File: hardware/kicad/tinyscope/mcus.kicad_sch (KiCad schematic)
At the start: 22 parts, among them SW1 SW_SPST, U10 STM32H753VITx, X1 25MHz

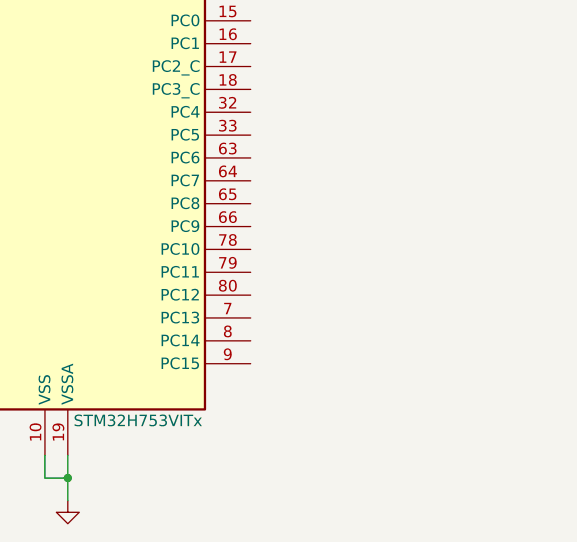
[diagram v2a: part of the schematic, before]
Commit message: feat: hardware: Add tinyscope kicad project. Adds LSE XTAL. Missing capacitor values
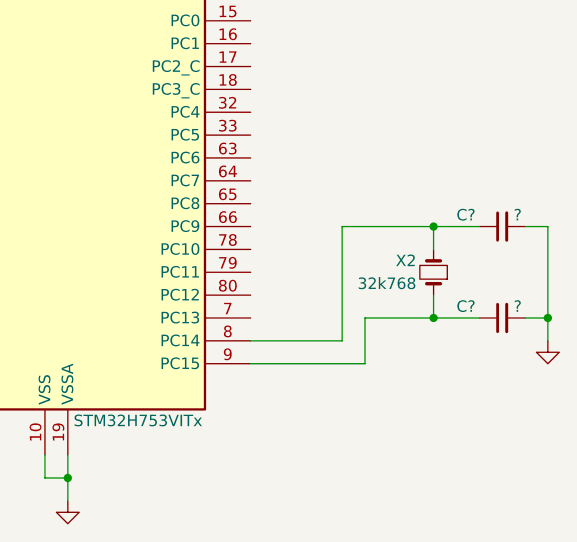
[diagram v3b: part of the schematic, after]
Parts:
- added C? (x2): ?, symbol Device:C_Small
- added X2: 32k768, symbol Device:Crystal_Small
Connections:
- net GND: now also C?.2, C?.2
- net at U10.8 (PC14): now also C?.1, X2.2
- net at U10.9 (PC15): now also C?.1, X2.1
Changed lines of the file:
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@@
   (junction (at 83.82 60.96) (diameter 0) (color 0 0 0 0)
   )
+  (junction (at 175.26 160.02) (diameter 0) (color 0 0 0 0)
+  )
   (junction (at 50.8 33.02) (diameter 0) (color 0 0 0 0)
   )
@@
   (junction (at 71.12 33.02) (diameter 0) (color 0 0 0 0)
   )
+  (junction (at 187.96 160.02) (diameter 0) (color 0 0 0 0)
+  )
   (junction (at 40.64 22.86) (diameter 0) (color 0 0 0 0)
   )
@@
   (junction (at 60.96 22.86) (diameter 0) (color 0 0 0 0)
   )
+  (junction (at 175.26 149.86) (diameter 0) (color 0 0 0 0)
+  )
   (junction (at 157.48 22.86) (diameter 0) (color 0 0 0 0)
   )
@@
     (stroke (width 0) (type default))
   )
+  (wire (pts (xy 175.26 149.86) (xy 180.34 149.86))
+    (stroke (width 0) (type default))
+  )
   (wire (pts (xy 40.64 33.02) (xy 30.48 33.02))
     (stroke (width 0) (type default))
   )
+  (wire (pts (xy 185.42 149.86) (xy 187.96 149.86))
+    (stroke (width 0) (type default))
+  )
   (wire (pts (xy 55.88 58.42) (xy 55.88 60.96))
     (stroke (width 0) (type default))
@@
     (stroke (width 0) (type default))
   )
+  (wire (pts (xy 187.96 149.86) (xy 187.96 160.02))
+    (stroke (width 0) (type default))
+  )
   (wire (pts (xy 30.48 40.64) (xy 30.48 45.72))
     (stroke (width 0) (type default))
@@
     (stroke (width 0) (type default))
   )
+  (wire (pts (xy 175.26 160.02) (xy 180.34 160.02))
+    (stroke (width 0) (type default))
+  )
   (wire (pts (xy 134.62 175.26) (xy 134.62 177.8))
     (stroke (width 0) (type default))
@@
     (stroke (width 0) (type default))
   )
+  (wire (pts (xy 187.96 160.02) (xy 187.96 162.56))
+    (stroke (width 0) (type default))
+  )
+  (wire (pts (xy 175.26 149.86) (xy 175.26 152.4))
+    (stroke (width 0) (type default))
+  )
   (wire (pts (xy 157.48 33.02) (xy 167.64 33.02))
     (stroke (width 0) (type default))
   )
+  (wire (pts (xy 175.26 157.48) (xy 175.26 160.02))
+    (stroke (width 0) (type default))
+  )
+  (wire (pts (xy 154.94 162.56) (xy 165.1 162.56))
+    (stroke (width 0) (type default))
+  )
   (wire (pts (xy 50.8 22.86) (xy 50.8 25.4))
     (stroke (width 0) (type default))
@@
     (stroke (width 0) (type default))
   )
+  (wire (pts (xy 165.1 149.86) (xy 165.1 162.56))
+    (stroke (width 0) (type default))
+  )
   (wire (pts (xy 96.52 162.56) (xy 96.52 165.1))
     (stroke (width 0) (type default))
@@
     (stroke (width 0) (type default))
   )
+  (wire (pts (xy 175.26 160.02) (xy 167.64 160.02))
+    (stroke (width 0) (type default))
+  )
   (wire (pts (xy 99.06 30.48) (xy 109.22 30.48))
     (stroke (width 0) (type default))
@@
     (stroke (width 0) (type default))
   )
+  (wire (pts (xy 167.64 160.02) (xy 167.64 165.1))
+    (stroke (width 0) (type default))
+  )
   (wire (pts (xy 93.98 53.34) (xy 96.52 53.34))
     (stroke (width 0) (type default))
@@
     (stroke (width 0) (type default))
   )
+  (wire (pts (xy 175.26 149.86) (xy 165.1 149.86))
+    (stroke (width 0) (type default))
+  )
   (wire (pts (xy 106.68 160.02) (xy 106.68 162.56))
     (stroke (width 0) (type default))
@@
     (stroke (width 0) (type default))
   )
+  (wire (pts (xy 185.42 160.02) (xy 187.96 160.02))
+    (stroke (width 0) (type default))
+  )
   (wire (pts (xy 66.04 58.42) (xy 66.04 60.96))
     (stroke (width 0) (type default))
@@
   )
   (wire (pts (xy 71.12 33.02) (xy 71.12 30.48))
+    (stroke (width 0) (type default))
+  )
+  (wire (pts (xy 167.64 165.1) (xy 154.94 165.1))
     (stroke (width 0) (type default))
   )
@@
     )
   )
+  (symbol (lib_id "Device:Crystal_Small") (at 175.26 154.94 90) (unit 1)
+    (in_bom yes) (on_board yes) (dnp no)
+    (property "Reference" "X2" (at 173.355 153.67 90)
+      (effects (font (size 1.27 1.27)) (justify left))
+    )
+    (property "Value" "32k768" (at 173.355 156.21 90)
+      (effects (font (size 1.27 1.27)) (justify left))
+    )
+    (property "Footprint" "" (at 175.26 154.94 0)
+      (effects (font (size 1.27 1.27)) hide)
+    )
+    (property "Datasheet" "~" (at 175.26 154.94 0)
+      (effects (font (size 1.27 1.27)) hide)
+    )
+    (pin "1")
+    (pin "2")
+    (instances
+      (project "tinyscope"
+        (path "/bb072e32-cc57-415a-8554-0e84d374f333/f3c865ab-23cb-49a1-bb6d-4ee24e55c7fa"
+          (reference "X2") (unit 1)
+        )
+      )
+    )
+  )
   (symbol (lib_id "Device:Crystal_Small") (at 96.52 57.15 90) (unit 1)
     (in_bom yes) (on_board yes) (dnp no) (fields_autoplaced)
@@
     )
   )
+  (symbol (lib_id "Device:C_Small") (at 182.88 149.86 90) (mirror x) (unit 1)
+    (in_bom yes) (on_board yes) (dnp no)
+    (property "Reference" "C?" (at 177.8 148.59 90)
+      (effects (font (size 1.27 1.27)) (justify right))
+    )
+    (property "Value" "?" (at 184.15 148.59 90)
+      (effects (font (size 1.27 1.27)) (justify right))
+    )
+    (property "Footprint" "" (at 182.88 149.86 0)
+      (effects (font (size 1.27 1.27)) hide)
+    )
+    (property "Datasheet" "~" (at 182.88 149.86 0)
+      (effects (font (size 1.27 1.27)) hide)
+    )
+    (pin "1")
+    (pin "2")
+    (instances
+      (project "tinyscope"
+        (path "/bb072e32-cc57-415a-8554-0e84d374f333"
+          (reference "C?") (unit 1)
+        )
+        (path "/bb072e32-cc57-415a-8554-0e84d374f333/7c1b1425-60eb-4f71-b125-42ba246f39fb"
+          (reference "C1") (unit 1)
+        )
+        (path "/bb072e32-cc57-415a-8554-0e84d374f333/f3c865ab-23cb-49a1-bb6d-4ee24e55c7fa"
+          (reference "C43") (unit 1)
+        )
+      )
+    )
+  )
   (symbol (lib_id "power:GND") (at 20.32 63.5 0) (mirror y) (unit 1)
     (in_bom yes) (on_board yes) (dnp no) (fields_autoplaced)
@@
     )
   )
+  (symbol (lib_id "power:GND") (at 187.96 162.56 0) (mirror y) (unit 1)
+    (in_bom yes) (on_board yes) (dnp no) (fields_autoplaced)
+    (property "Reference" "#PWR?" (at 187.96 168.91 0)
+      (effects (font (size 1.27 1.27)) hide)
+    )
+    (property "Value" "GND" (at 187.96 167.64 0)
+      (effects (font (size 1.27 1.27)) hide)
+    )
+    (property "Footprint" "" (at 187.96 162.56 0)
+      (effects (font (size 1.27 1.27)) hide)
+    )
+    (property "Datasheet" "" (at 187.96 162.56 0)
+      (effects (font (size 1.27 1.27)) hide)
+    )
+    (pin "1")
+    (instances
+      (project "tinyscope"
+        (path "/bb072e32-cc57-415a-8554-0e84d374f333"
+          (reference "#PWR?") (unit 1)
+        )
+        (path "/bb072e32-cc57-415a-8554-0e84d374f333/1c26ba79-0794-42b8-82e1-265696d83365"
+          (reference "#PWR034") (unit 1)
+        )
+        (path "/bb072e32-cc57-415a-8554-0e84d374f333/f3c865ab-23cb-49a1-bb6d-4ee24e55c7fa"
+          (reference "#PWR053") (unit 1)
+        )
+      )
+    )
+  )
   (symbol (lib_id "Device:C_Small") (at 81.28 27.94 0) (mirror y) (unit 1)
     (in_bom yes) (on_board yes) (dnp no)
@@
         )
       )
+    )
+  )
+  (symbol (lib_id "Device:C_Small") (at 182.88 160.02 90) (mirror x) (unit 1)
+    (in_bom yes) (on_board yes) (dnp no)
+    (property "Reference" "C?" (at 177.8 158.75 90)
+      (effects (font (size 1.27 1.27)) (justify right))
+    )
+    (property "Value" "?" (at 184.15 158.75 90)
+      (effects (font (size 1.27 1.27)) (justify right))
+    )
+    (property "Footprint" "" (at 182.88 160.02 0)
+      (effects (font (size 1.27 1.27)) hide)
+    )
+    (property "Datasheet" "~" (at 182.88 160.02 0)
+      (effects (font (size 1.27 1.27)) hide)
+    )
+    (pin "1")
+    (pin "2")
+    (instances
+      (project "tinyscope"
+        (path "/bb072e32-cc57-415a-8554-0e84d374f333"
+          (reference "C?") (unit 1)
+        )
+        (path "/bb072e32-cc57-415a-8554-0e84d374f333/7c1b1425-60eb-4f71-b125-42ba246f39fb"
+          (reference "C1") (unit 1)
+        )
+        (path "/bb072e32-cc57-415a-8554-0e84d374f333/f3c865ab-23cb-49a1-bb6d-4ee24e55c7fa"
+          (reference "C44") (unit 1)
+        )
+      )
